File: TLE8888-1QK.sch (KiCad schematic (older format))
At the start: 40 parts, among them Q1 IPD30N06S2L-23, U2 TLE8888QK

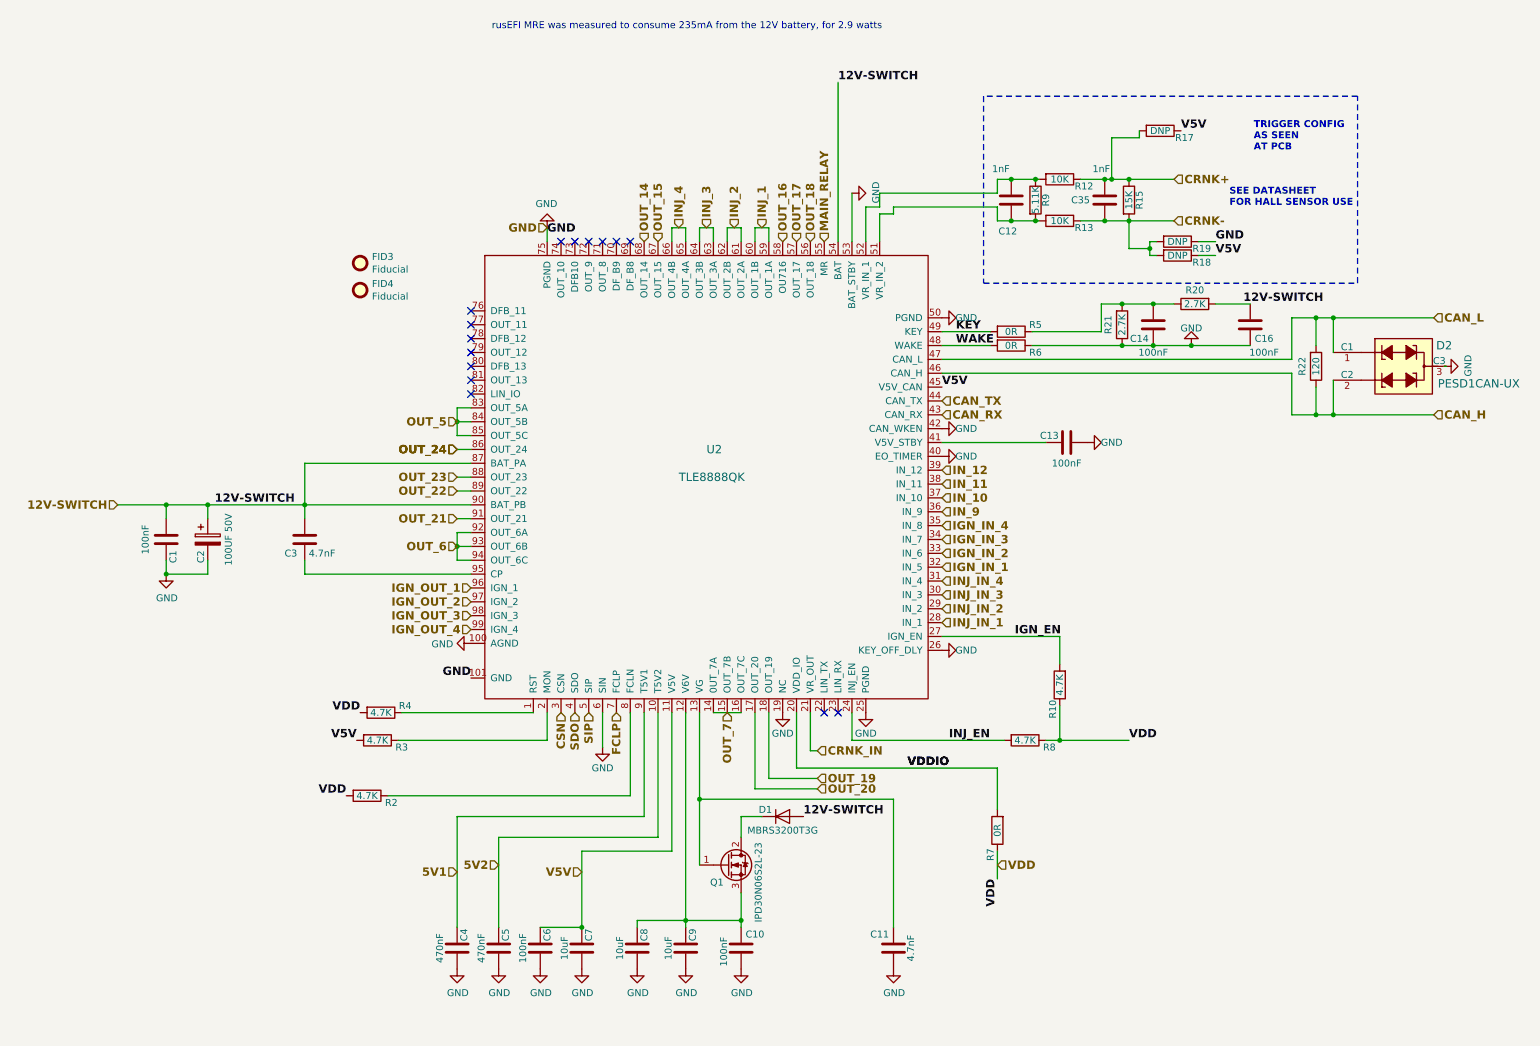
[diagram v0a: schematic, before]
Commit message: Updated 1k/1.5k resistor arrays, updated 2.7k's and R141. Changed several K's into k's for consistent ref designation names. https://github.com/rusefi/hw_microRusEfi/issues/51
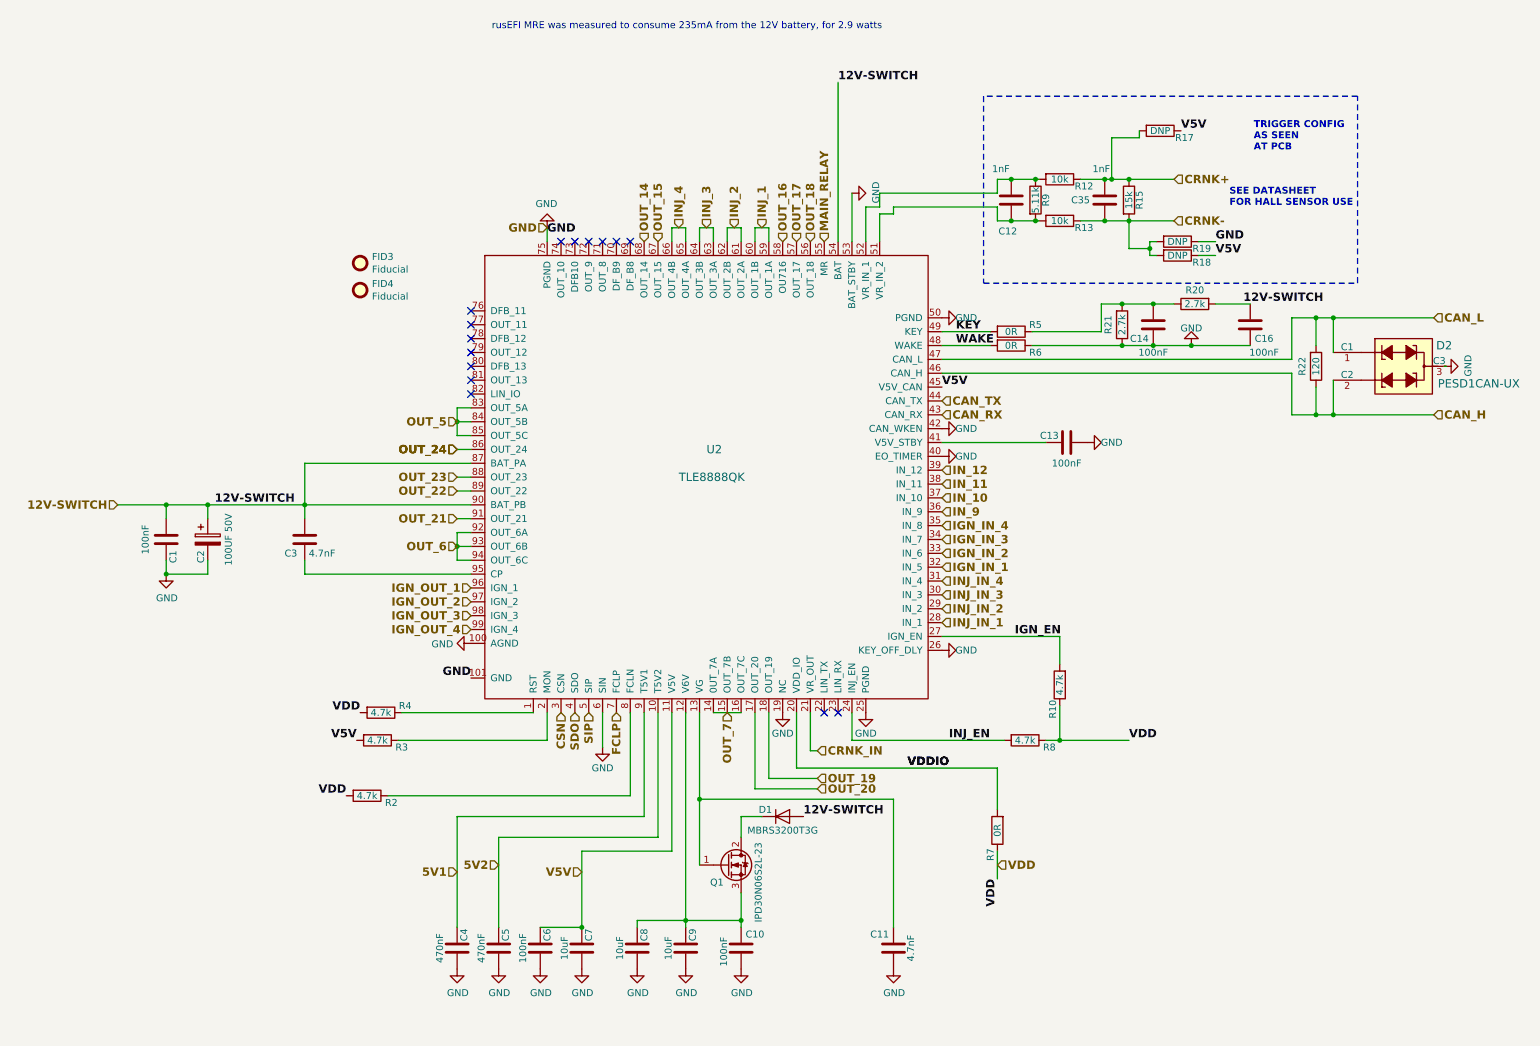
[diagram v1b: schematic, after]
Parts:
- R10, R2, R3, R4, R8: value 4.7K -> 4.7k
- R12, R13: value 10K -> 10k
- R15: value 15K -> 15k
- R20, R21: value 2.7K -> 2.7k; Part # RMCF0603JT2K70 -> RMCF0603FT2K70; VEND# RMCF0603JT2K70CT-ND -> RMCF0603FT2K70CT-ND
- R9: value 5.11K -> 5.11k
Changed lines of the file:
@@
 P 12175 6400
 F 0 "R9" V 12250 6400 50  0000 C CNN
-F 1 "5.11K" V 12175 6400 50  0000 C CNN
+F 1 "5.11k" V 12175 6400 50  0000 C CNN
 F 2 "Resistor_SMD:R_0603_1608Metric" V 12105 6400 50  0001 C CNN
 F 3 "~" H 12175 6400 50  0001 C CNN
@@
 P 12350 6250
 F 0 "R12" V 12400 6425 50  0000 C CNN
-F 1 "10K" V 12350 6250 50  0000 C CNN
+F 1 "10k" V 12350 6250 50  0000 C CNN
 F 2 "Resistor_SMD:R_0603_1608Metric" V 12280 6250 50  0001 C CNN
-F 3 "~" H 12350 6250 50  0001 C CNN
+F 3 "TBD" H 12350 6250 50  0001 C CNN
 F 4 "RMCF0603JT10K0" H -100 0   50  0001 C CNN "Part #"
 F 5 "DIGI" H -100 0   50  0001 C CNN "VEND"
@@
 P 12350 6550
 F 0 "R13" V 12400 6725 50  0000 C CNN
-F 1 "10K" V 12350 6550 50  0000 C CNN
+F 1 "10k" V 12350 6550 50  0000 C CNN
 F 2 "Resistor_SMD:R_0603_1608Metric" V 12280 6550 50  0001 C CNN
-F 3 "~" H 12350 6550 50  0001 C CNN
+F 3 "TBD" H 12350 6550 50  0001 C CNN
 F 4 "RMCF0603JT10K0" H -100 0   50  0001 C CNN "Part #"
 F 5 "DIGI" H -100 0   50  0001 C CNN "VEND"
@@
 P 7425 10300
 F 0 "R3" V 7475 10475 50  0000 C CNN
-F 1 "4.7K" V 7425 10300 50  0000 C CNN
+F 1 "4.7k" V 7425 10300 50  0000 C CNN
 F 2 "Resistor_SMD:R_0603_1608Metric" V 7355 10300 50  0001 C CNN
 F 3 "~" H 7425 10300 50  0001 C CNN
@@
 P 7450 10100
 F 0 "R4" V 7400 10275 50  0000 C CNN
-F 1 "4.7K" V 7450 10100 50  0000 C CNN
+F 1 "4.7k" V 7450 10100 50  0000 C CNN
 F 2 "Resistor_SMD:R_0603_1608Metric" V 7380 10100 50  0001 C CNN
 F 3 "~" H 7450 10100 50  0001 C CNN
@@
 P 7350 10700
 F 0 "R2" V 7400 10875 50  0000 C CNN
-F 1 "4.7K" V 7350 10700 50  0000 C CNN
+F 1 "4.7k" V 7350 10700 50  0000 C CNN
 F 2 "Resistor_SMD:R_0603_1608Metric" V 7280 10700 50  0001 C CNN
 F 3 "~" H 7350 10700 50  0001 C CNN
@@
 P 12800 7300
 F 0 "R21" V 12700 7300 50  0000 C CNN
-F 1 "2.7K" V 12800 7300 50  0000 C CNN
+F 1 "2.7k" V 12800 7300 50  0000 C CNN
 F 2 "Resistor_SMD:R_0603_1608Metric" V 12730 7300 50  0001 C CNN
 F 3 "~" H 12800 7300 50  0001 C CNN
-F 4 "RMCF0603JT2K70" H 0   0   50  0001 C CNN "Part #"
-F 5 "DIGI" H 0   0   50  0001 C CNN "VEND"
-F 6 "RMCF0603JT2K70CT-ND" H 0   0   50  0001 C CNN "VEND#"
+F 4 "RMCF0603FT2K70" H 0   0   50  0001 C CNN "Part #"
+F 5 "DIGI" H 0   0   50  0001 C CNN "VEND"
+F 6 "RMCF0603FT2K70CT-ND" H 0   0   50  0001 C CNN "VEND#"
 F 7 "StackPole" H 0   0   50  0001 C CNN "Manufacturer"
 	1    12800 7300
@@
 P 13325 7150
 F 0 "R20" V 13225 7150 50  0000 C CNN
-F 1 "2.7K" V 13325 7150 50  0000 C CNN
+F 1 "2.7k" V 13325 7150 50  0000 C CNN
 F 2 "Resistor_SMD:R_0603_1608Metric" V 13255 7150 50  0001 C CNN
 F 3 "~" H 13325 7150 50  0001 C CNN
-F 4 "RMCF0603JT2K70" H 0   0   50  0001 C CNN "Part #"
-F 5 "DIGI" H 0   0   50  0001 C CNN "VEND"
-F 6 "RMCF0603JT2K70CT-ND" H 0   0   50  0001 C CNN "VEND#"
+F 4 "RMCF0603FT2K70" H 0   0   50  0001 C CNN "Part #"
+F 5 "DIGI" H 0   0   50  0001 C CNN "VEND"
+F 6 "RMCF0603FT2K70CT-ND" H 0   0   50  0001 C CNN "VEND#"
 F 7 "StackPole" H 0   0   50  0001 C CNN "Manufacturer"
 	1    13325 7150
@@
 P 12100 10300
 F 0 "R8" V 12150 10475 50  0000 C CNN
-F 1 "4.7K" V 12100 10300 50  0000 C CNN
+F 1 "4.7k" V 12100 10300 50  0000 C CNN
 F 2 "Resistor_SMD:R_0603_1608Metric" V 12030 10300 50  0001 C CNN
 F 3 "~" H 12100 10300 50  0001 C CNN
@@
 P 12350 9900
 F 0 "R10" V 12400 10075 50  0000 C CNN
-F 1 "4.7K" V 12350 9900 50  0000 C CNN
+F 1 "4.7k" V 12350 9900 50  0000 C CNN
 F 2 "Resistor_SMD:R_0603_1608Metric" V 12280 9900 50  0001 C CNN
 F 3 "~" H 12350 9900 50  0001 C CNN
@@
 P 12850 6400
 F 0 "R15" V 12925 6400 50  0000 C CNN
-F 1 "15K" V 12850 6400 50  0000 C CNN
+F 1 "15k" V 12850 6400 50  0000 C CNN
 F 2 "Resistor_SMD:R_0603_1608Metric" V 12780 6400 50  0001 C CNN
 F 3 "~" H 12850 6400 50  0001 C CNN

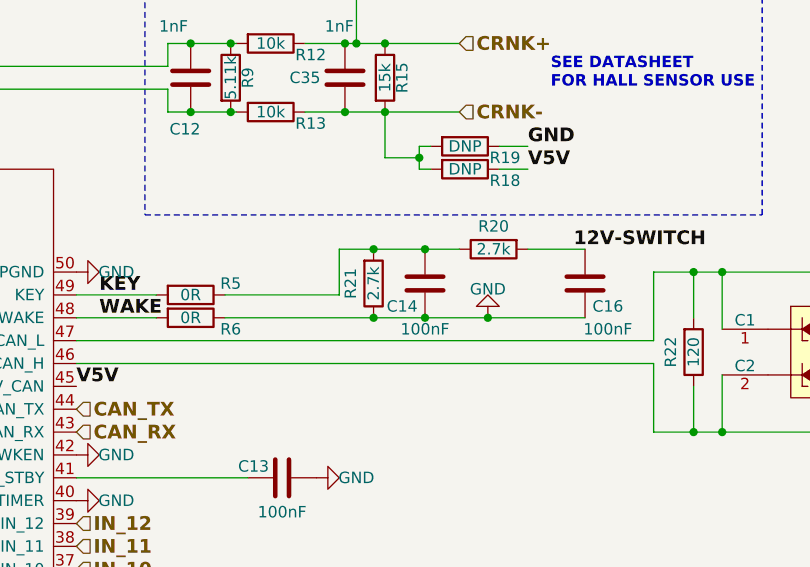
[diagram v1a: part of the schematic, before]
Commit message: Moved R21 to match position as noted on demo board reference design. https://github.com/rusefi/hw_microRusEfi/issues/93
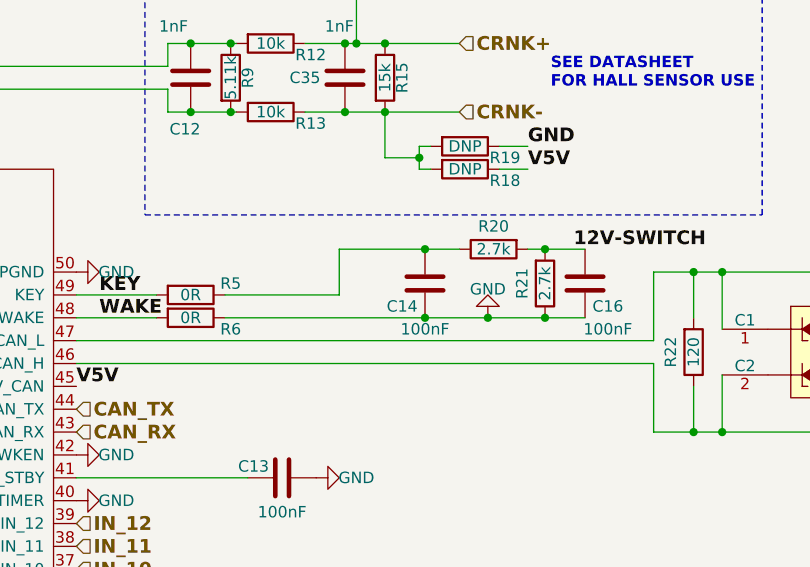
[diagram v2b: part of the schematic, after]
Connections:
- net 12V-SWITCH: now also R21.2
- net at C14.1, R20.1, R5.1: no longer R21.2
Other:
- moved on the sheet: R21
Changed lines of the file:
@@
 L Device:R R21
 U 1 1 5D310735
-P 12800 7300
-F 0 "R21" V 12700 7300 50  0000 C CNN
-F 1 "2.7k" V 12800 7300 50  0000 C CNN
-F 2 "Resistor_SMD:R_0603_1608Metric" V 12730 7300 50  0001 C CNN
-F 3 "~" H 12800 7300 50  0001 C CNN
-F 4 "RMCF0603FT2K70" H 0   0   50  0001 C CNN "Part #"
-F 5 "DIGI" H 0   0   50  0001 C CNN "VEND"
-F 6 "RMCF0603FT2K70CT-ND" H 0   0   50  0001 C CNN "VEND#"
-F 7 "StackPole" H 0   0   50  0001 C CNN "Manufacturer"
-	1    12800 7300
+P 13550 7300
+F 0 "R21" V 13450 7300 50  0000 C CNN
+F 1 "2.7k" V 13550 7300 50  0000 C CNN
+F 2 "Resistor_SMD:R_0603_1608Metric" V 13480 7300 50  0001 C CNN
+F 3 "~" H 13550 7300 50  0001 C CNN
+F 4 "RMCF0603FT2K70" H 750 0   50  0001 C CNN "Part #"
+F 5 "DIGI" H 750 0   50  0001 C CNN "VEND"
+F 6 "RMCF0603FT2K70CT-ND" H 750 0   50  0001 C CNN "VEND#"
+F 7 "StackPole" H 750 0   50  0001 C CNN "Manufacturer"
+	1    13550 7300
 	1    0    0    1
 $EndComp
@@
 	12650 7350 12650 7150
 Wire Wire Line
-	12650 7150 12800 7150
-Wire Wire Line
 	11500 7350 11850 7350
 Connection ~ 13025 7150
-Wire Wire Line
-	13025 7450 12800 7450
 Connection ~ 13025 7450
 Wire Wire Line
@@
 Wire Wire Line
 	12850 6550 12850 6750
-Connection ~ 12800 7150
-Wire Wire Line
-	12800 7150 13025 7150
-Connection ~ 12800 7450
-Wire Wire Line
-	12800 7450 12150 7450
-Wire Wire Line
-	13300 7450 13725 7450
-Wire Wire Line
-	13475 7150 13725 7150
+Wire Wire Line
+	13300 7450 13550 7450
+Wire Wire Line
+	13475 7150 13550 7150
 Wire Notes Line
 	14500 5650 11800 5650
@@
 Wire Wire Line
 	10550 10375 10600 10375
+Connection ~ 13550 7450
+Wire Wire Line
+	13550 7450 13725 7450
+Connection ~ 13550 7150
+Wire Wire Line
+	13550 7150 13725 7150
+Wire Wire Line
+	12650 7150 13025 7150
+Wire Wire Line
+	12150 7450 13025 7450
 $EndSCHEMATC

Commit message: R0.3 released
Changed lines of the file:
@@
 	1    0    0    -1
 $EndComp
-Text Notes 8250 5175 0    50   ~ 0
+Text Notes 8250 5175 0    50   ~ 6
 rusEFI MRE was measured to consume 235mA from the 12V battery, for 2.9 watts
 Text HLabel 10600 10375 2    60   Input ~ 12

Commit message: BOM fix, reset button
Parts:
- C11, C3: Manufacturer AVX -> TDK; Part # 06031A470JAT2A -> CGA3E2X7R1H472K080AA; VEND# 478-1144-1-ND -> 445-5661-1-ND
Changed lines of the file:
@@
 EESchema Schematic File Version 4
 LIBS:microRusEfi-cache
-EELAYER 29 0
+EELAYER 30 0
 EELAYER END
 $Descr User 19685 15748
@@
 F 3 "~" H 6900 8850 50  0001 C CNN
 F 4 "DIGI" H 0   0   50  0001 C CNN "VEND"
-F 5 "06031A470JAT2A" H 0   0   50  0001 C CNN "Part #"
-F 6 "478-1144-1-ND" H 0   0   50  0001 C CNN "VEND#"
-F 7 "AVX" H 0   0   50  0001 C CNN "Manufacturer"
+F 5 "CGA3E2X7R1H472K080AA" H 0   0   50  0001 C CNN "Part #"
+F 6 "445-5661-1-ND" H 0   0   50  0001 C CNN "VEND#"
+F 7 "TDK" H 0   0   50  0001 C CNN "Manufacturer"
 	1    6900 8850
 	1    0    0    -1
@@
 F 3 "~" H 11150 11800 50  0001 C CNN
 F 4 "DIGI" H 650 100 50  0001 C CNN "VEND"
-F 5 "06031A470JAT2A" H 0   0   50  0001 C CNN "Part #"
-F 6 "478-1144-1-ND" H 0   0   50  0001 C CNN "VEND#"
-F 7 "AVX" H 0   0   50  0001 C CNN "Manufacturer"
+F 5 "CGA3E2X7R1H472K080AA" H 0   0   50  0001 C CNN "Part #"
+F 6 "445-5661-1-ND" H 0   0   50  0001 C CNN "VEND#"
+F 7 "TDK" H 0   0   50  0001 C CNN "Manufacturer"
 	1    11150 11800
 	1    0    0    -1
@@
 	1    0    0    -1
 $EndComp
-Text Notes 8250 5175 0    50   ~ 6
+Text Notes 8250 5175 0    50   ~ 10
 rusEFI MRE was measured to consume 235mA from the 12V battery, for 2.9 watts
 Text HLabel 10600 10375 2    60   Input ~ 12
